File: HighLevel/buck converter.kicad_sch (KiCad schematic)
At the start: 11 parts, among them U12 LM5161PWP

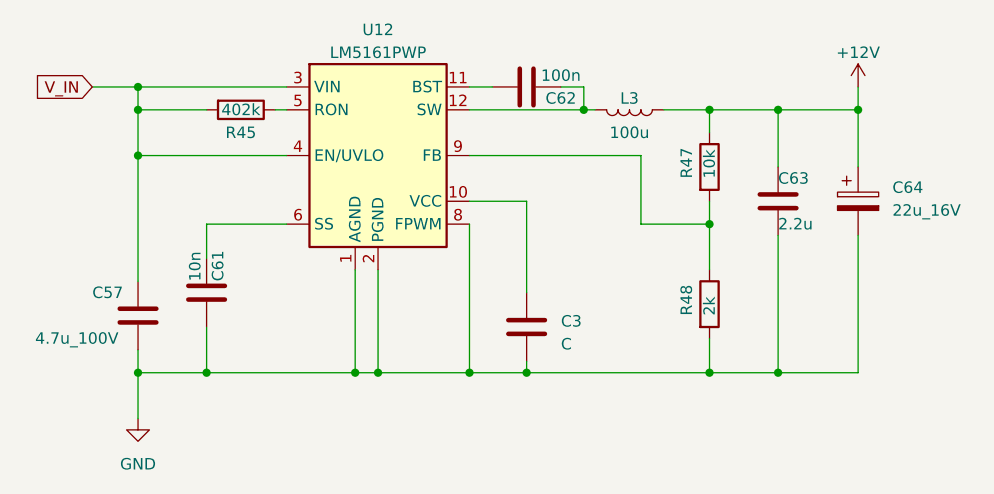
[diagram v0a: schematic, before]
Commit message: Added last two sheets and some footprints
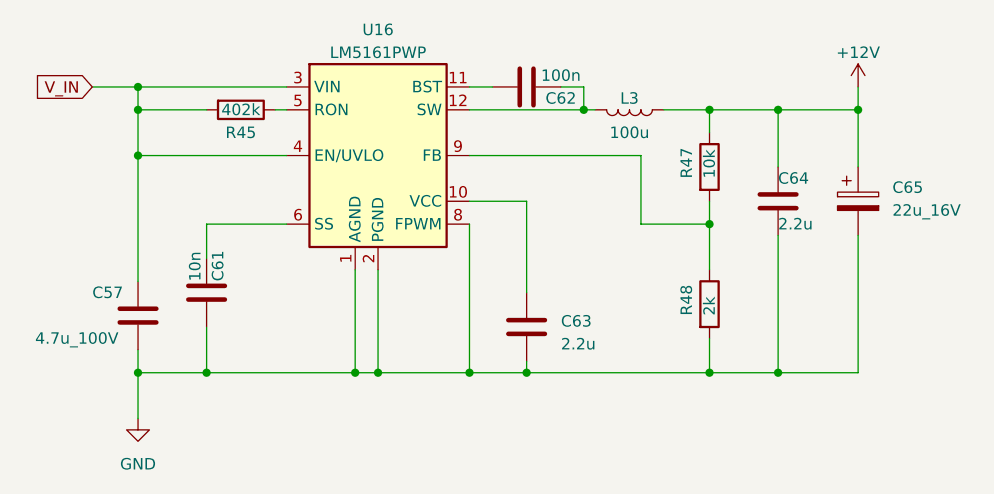
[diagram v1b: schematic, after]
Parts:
- C57, C61, C62: footprint (none) -> Capacitor_SMD:C_0805_2012Metric
- C63: renamed from C3; value C -> 2.2u; footprint (none) -> Capacitor_SMD:C_0805_2012Metric
- C64: renamed from C63; footprint (none) -> Capacitor_SMD:C_0805_2012Metric
- C65: renamed from C64; footprint (none) -> Capacitor_SMD:CP_Elec_6.3x7.7
- L3: footprint (none) -> Inductor_SMD:L_0805_2012Metric
- R45, R47, R48: footprint (none) -> Resistor_SMD:R_0805_2012Metric
- renumbered U12 to U16
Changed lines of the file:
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@@
   (symbol (lib_id "Device:C") (at 162.56 107.95 0) (unit 1)
     (in_bom yes) (on_board yes) (dnp no) (fields_autoplaced)
-    (property "Reference" "C3" (at 166.37 107.315 0)
-      (effects (font (size 1.27 1.27)) (justify left))
-    )
-    (property "Value" "C" (at 166.37 109.855 0)
-      (effects (font (size 1.27 1.27)) (justify left))
-    )
-    (property "Footprint" "" (at 163.5252 111.76 0)
+    (property "Reference" "C63" (at 166.37 107.315 0)
+      (effects (font (size 1.27 1.27)) (justify left))
+    )
+    (property "Value" "2.2u" (at 166.37 109.855 0)
+      (effects (font (size 1.27 1.27)) (justify left))
+    )
+    (property "Footprint" "Capacitor_SMD:C_0805_2012Metric" (at 163.5252 111.76 0)
       (effects (font (size 1.27 1.27)) hide)
     )
@@
     (pin "2")
     (instances
+      (project "HighLevel"
+        (path "/26149e3f-2822-4531-a73b-0a61b71078cc/65b28eab-109a-4dc4-85fe-9cab4996bf20"
+          (reference "C63") (unit 1)
+        )
+      )
       (project "buck converter"
         (path "/b8f0b334-0d62-49d6-b283-2fb97ebb9ee5"
@@
       (effects (font (size 1.27 1.27)))
     )
-    (property "Footprint" "" (at 173.99 83.82 0)
+    (property "Footprint" "Inductor_SMD:L_0805_2012Metric" (at 173.99 83.82 0)
       (effects (font (size 1.27 1.27)) hide)
     )
@@
     (pin "2")
     (instances
-      (project "buck converter"
-        (path "/b8f0b334-0d62-49d6-b283-2fb97ebb9ee5"
+      (project "HighLevel"
+        (path "/26149e3f-2822-4531-a73b-0a61b71078cc/65b28eab-109a-4dc4-85fe-9cab4996bf20"
           (reference "L3") (unit 1)
         )
       )
+      (project "buck converter"
+        (path "/b8f0b334-0d62-49d6-b283-2fb97ebb9ee5"
+          (reference "L3") (unit 1)
+        )
+      )
     )
   )
   (symbol (lib_id "Device:C_Polarized") (at 199.39 93.98 0) (unit 1)
     (in_bom yes) (on_board yes) (dnp no) (fields_autoplaced)
-    (property "Reference" "C64" (at 203.2 92.456 0)
+    (property "Reference" "C65" (at 203.2 92.456 0)
       (effects (font (size 1.27 1.27)) (justify left))
     )
@@
       (effects (font (size 1.27 1.27)) (justify left))
     )
-    (property "Footprint" "" (at 200.3552 97.79 0)
+    (property "Footprint" "Capacitor_SMD:CP_Elec_6.3x7.7" (at 200.3552 97.79 0)
       (effects (font (size 1.27 1.27)) hide)
     )
@@
     (pin "2")
     (instances
+      (project "HighLevel"
+        (path "/26149e3f-2822-4531-a73b-0a61b71078cc/65b28eab-109a-4dc4-85fe-9cab4996bf20"
+          (reference "C65") (unit 1)
+        )
+      )
       (project "buck converter"
         (path "/b8f0b334-0d62-49d6-b283-2fb97ebb9ee5"
@@
   (symbol (lib_id "Regulator_Switching:LM5161PWP") (at 146.05 88.9 0) (unit 1)
     (in_bom yes) (on_board yes) (dnp no) (fields_autoplaced)
-    (property "Reference" "U12" (at 146.05 74.93 0)
+    (property "Reference" "U16" (at 146.05 74.93 0)
       (effects (font (size 1.27 1.27)))
     )
@@
     (pin "9")
     (instances
+      (project "HighLevel"
+        (path "/26149e3f-2822-4531-a73b-0a61b71078cc/65b28eab-109a-4dc4-85fe-9cab4996bf20"
+          (reference "U16") (unit 1)
+        )
+      )
       (project "buck converter"
         (path "/b8f0b334-0d62-49d6-b283-2fb97ebb9ee5"
@@
       (effects (font (size 1.27 1.27)) (justify left))
     )
-    (property "Footprint" "" (at 181.102 105.41 90)
+    (property "Footprint" "Resistor_SMD:R_0805_2012Metric" (at 181.102 105.41 90)
       (effects (font (size 1.27 1.27)) hide)
     )
@@
     (pin "2")
     (instances
-      (project "buck converter"
-        (path "/b8f0b334-0d62-49d6-b283-2fb97ebb9ee5"
+      (project "HighLevel"
+        (path "/26149e3f-2822-4531-a73b-0a61b71078cc/65b28eab-109a-4dc4-85fe-9cab4996bf20"
           (reference "R48") (unit 1)
         )
       )
+      (project "buck converter"
+        (path "/b8f0b334-0d62-49d6-b283-2fb97ebb9ee5"
+          (reference "R48") (unit 1)
+        )
+      )
     )
   )
@@
       (effects (font (size 1.27 1.27)) (justify left))
     )
-    (property "Footprint" "" (at 120.3452 110.49 0)
+    (property "Footprint" "Capacitor_SMD:C_0805_2012Metric" (at 120.3452 110.49 0)
       (effects (font (size 1.27 1.27)) hide)
     )
@@
     (pin "2")
     (instances
-      (project "buck converter"
-        (path "/b8f0b334-0d62-49d6-b283-2fb97ebb9ee5"
+      (project "HighLevel"
+        (path "/26149e3f-2822-4531-a73b-0a61b71078cc/65b28eab-109a-4dc4-85fe-9cab4996bf20"
           (reference "C57") (unit 1)
         )
       )
+      (project "buck converter"
+        (path "/b8f0b334-0d62-49d6-b283-2fb97ebb9ee5"
+          (reference "C57") (unit 1)
+        )
+      )
     )
   )
   (symbol (lib_id "power:GND") (at 119.38 118.11 0) (unit 1)
     (in_bom yes) (on_board yes) (dnp no) (fields_autoplaced)
-    (property "Reference" "#PWR01" (at 119.38 124.46 0)
+    (property "Reference" "#PWR092" (at 119.38 124.46 0)
       (effects (font (size 1.27 1.27)) hide)
     )
@@
     (pin "1")
     (instances
+      (project "HighLevel"
+        (path "/26149e3f-2822-4531-a73b-0a61b71078cc/65b28eab-109a-4dc4-85fe-9cab4996bf20"
+          (reference "#PWR092") (unit 1)
+        )
+      )
       (project "buck converter"
         (path "/b8f0b334-0d62-49d6-b283-2fb97ebb9ee5"
@@
       (effects (font (size 1.27 1.27)) (justify left))
     )
-    (property "Footprint" "" (at 127.9652 107.95 0)
+    (property "Footprint" "Capacitor_SMD:C_0805_2012Metric" (at 127.9652 107.95 0)
       (effects (font (size 1.27 1.27)) hide)
     )
@@
     (pin "2")
     (instances
-      (project "buck converter"
-        (path "/b8f0b334-0d62-49d6-b283-2fb97ebb9ee5"
+      (project "HighLevel"
+        (path "/26149e3f-2822-4531-a73b-0a61b71078cc/65b28eab-109a-4dc4-85fe-9cab4996bf20"
           (reference "C61") (unit 1)
         )
       )
+      (project "buck converter"
+        (path "/b8f0b334-0d62-49d6-b283-2fb97ebb9ee5"
+          (reference "C61") (unit 1)
+        )
+      )
     )
   )
@@
       (effects (font (size 1.27 1.27)))
     )
-    (property "Footprint" "" (at 130.81 82.042 90)
+    (property "Footprint" "Resistor_SMD:R_0805_2012Metric" (at 130.81 82.042 90)
       (effects (font (size 1.27 1.27)) hide)
     )
@@
     (pin "2")
     (instances
-      (project "buck converter"
-        (path "/b8f0b334-0d62-49d6-b283-2fb97ebb9ee5"
+      (project "HighLevel"
+        (path "/26149e3f-2822-4531-a73b-0a61b71078cc/65b28eab-109a-4dc4-85fe-9cab4996bf20"
           (reference "R45") (unit 1)
         )
       )
+      (project "buck converter"
+        (path "/b8f0b334-0d62-49d6-b283-2fb97ebb9ee5"
+          (reference "R45") (unit 1)
+        )
+      )
     )
   )
   (symbol (lib_id "Device:C") (at 190.5 93.98 0) (unit 1)
     (in_bom yes) (on_board yes) (dnp no)
-    (property "Reference" "C63" (at 190.5 91.44 0)
+    (property "Reference" "C64" (at 190.5 91.44 0)
       (effects (font (size 1.27 1.27)) (justify left))
     )
@@
       (effects (font (size 1.27 1.27)) (justify left))
     )
-    (property "Footprint" "" (at 191.4652 97.79 0)
+    (property "Footprint" "Capacitor_SMD:C_0805_2012Metric" (at 191.4652 97.79 0)
       (effects (font (size 1.27 1.27)) hide)
     )
@@
     (pin "2")
     (instances
+      (project "HighLevel"
+        (path "/26149e3f-2822-4531-a73b-0a61b71078cc/65b28eab-109a-4dc4-85fe-9cab4996bf20"
+          (reference "C64") (unit 1)
+        )
+      )
       (project "buck converter"
         (path "/b8f0b334-0d62-49d6-b283-2fb97ebb9ee5"
@@
       (effects (font (size 1.27 1.27)) (justify left))
     )
-    (property "Footprint" "" (at 181.102 90.17 90)
+    (property "Footprint" "Resistor_SMD:R_0805_2012Metric" (at 181.102 90.17 90)
       (effects (font (size 1.27 1.27)) hide)
     )
@@
     (pin "2")
     (instances
-      (project "buck converter"
-        (path "/b8f0b334-0d62-49d6-b283-2fb97ebb9ee5"
+      (project "HighLevel"
+        (path "/26149e3f-2822-4531-a73b-0a61b71078cc/65b28eab-109a-4dc4-85fe-9cab4996bf20"
           (reference "R47") (unit 1)
         )
       )
+      (project "buck converter"
+        (path "/b8f0b334-0d62-49d6-b283-2fb97ebb9ee5"
+          (reference "R47") (unit 1)
+        )
+      )
     )
   )
@@
       (effects (font (size 1.27 1.27)))
     )
-    (property "Footprint" "" (at 158.75 82.2452 0)
+    (property "Footprint" "Capacitor_SMD:C_0805_2012Metric" (at 158.75 82.2452 0)
       (effects (font (size 1.27 1.27)) hide)
     )
@@
     (pin "2")
     (instances
-      (project "buck converter"
-        (path "/b8f0b334-0d62-49d6-b283-2fb97ebb9ee5"
+      (project "HighLevel"
+        (path "/26149e3f-2822-4531-a73b-0a61b71078cc/65b28eab-109a-4dc4-85fe-9cab4996bf20"
           (reference "C62") (unit 1)
         )
       )
+      (project "buck converter"
+        (path "/b8f0b334-0d62-49d6-b283-2fb97ebb9ee5"
+          (reference "C62") (unit 1)
+        )
+      )
     )
   )
   (symbol (lib_id "power:+12V") (at 199.39 81.28 0) (unit 1)
     (in_bom yes) (on_board yes) (dnp no) (fields_autoplaced)
-    (property "Reference" "#PWR02" (at 199.39 85.09 0)
+    (property "Reference" "#PWR093" (at 199.39 85.09 0)
       (effects (font (size 1.27 1.27)) hide)
     )
@@
     (pin "1")
     (instances
-      (project "buck converter"
-        (path "/b8f0b334-0d62-49d6-b283-2fb97ebb9ee5"
+      (project "HighLevel"
+        (path "/26149e3f-2822-4531-a73b-0a61b71078cc/65b28eab-109a-4dc4-85fe-9cab4996bf20"
+          (reference "#PWR093") (unit 1)
+        )
+      )
+      (project "buck converter"
+        (path "/b8f0b334-0d62-49d6-b283-2fb97ebb9ee5"
